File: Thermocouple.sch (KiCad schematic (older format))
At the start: 0 parts

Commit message: Blocked out the thermocouple worksheet
Added the instrumentation amplifier, ADC placeholder and general
temperature sensor placeholder.
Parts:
- added C?: C, ~, symbol C
- added D?: ZENER, ~, symbol ZENER
- added R? (x7): R, ~, symbol R
- added U? (x4): LM324, symbol LM324
- added U? (x2): MCP3550-60-E/SN, SO8, symbol MCP3550-60-E/SN
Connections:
- net labels added: +12V, -12V, AGND
- wire segments 0 -> 42
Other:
- note added: "16-24bit ADC\n\nIdeally, a two channel ADC, rather than\ntwo separate, discreet components: this \nand the device above."
- note added: "Acting as an instrumentation opamp"
- note added: "Input from physical \nthermocouple connector\n"
- note added: "Input from physical\nthermocouple connector\n"
- note added: "Zener placeholder for \ngeneral temperature sensor\n"

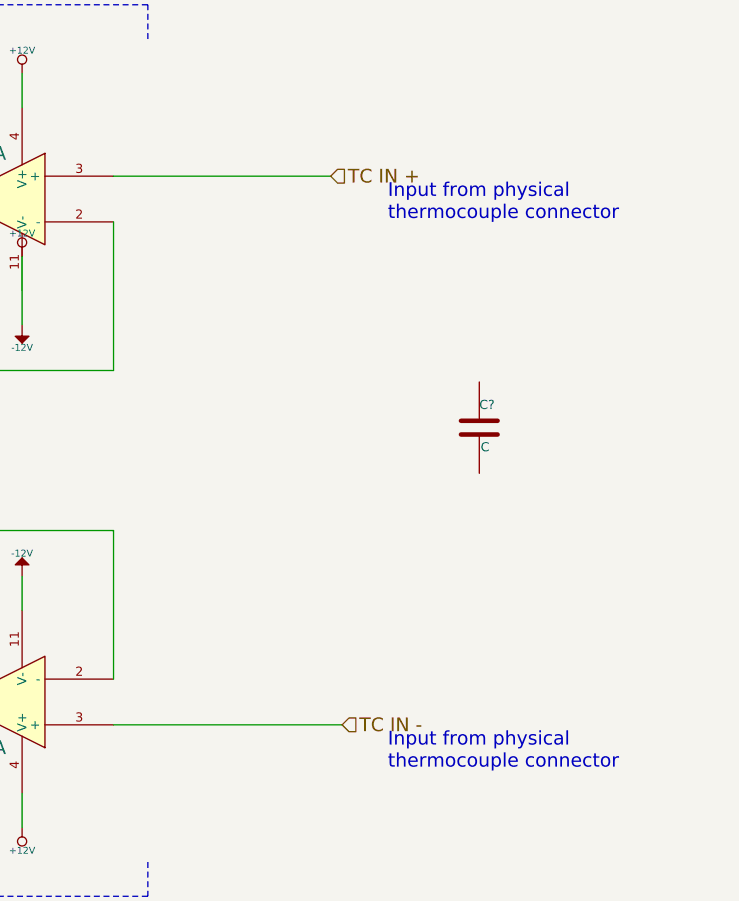
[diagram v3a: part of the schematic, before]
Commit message: Completed Arduino Block Diagram and Fan Redesign
The commits as of this are now up to date with the videos released for
Contextual Electronics, Week 3.
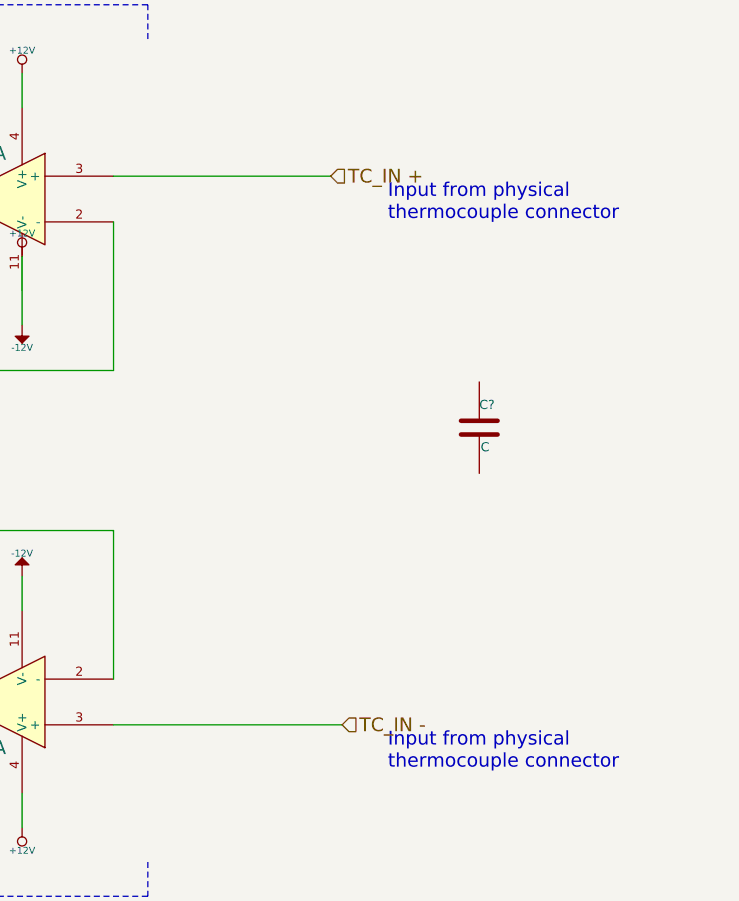
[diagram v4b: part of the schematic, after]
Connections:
- net labels added: TC_IN +, TC_IN -
- net labels removed: TC IN +, TC IN -
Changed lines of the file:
@@
 $Descr A4 11693 8268
 encoding utf-8
-Sheet 3 9
+Sheet 2 9
 Title ""
 Date "6 feb 2014"
@@
 $EndDescr
 Text HLabel 9100 2100 2    60   Input ~ 0
-TC IN +
+TC_IN +
 Text HLabel 9150 4500 2    60   Input ~ 0
-TC IN -
+TC_IN -
 Text HLabel 2050 3050 0    60   Input ~ 0
 MOSI

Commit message: Initial layout of relay and thermocouple
All block diagrams completed through Week 3.  Component selection
spreadsheets created: Bench Buddy Session 1CE.xlsx = official part
selection and bom.xlsx is the version I came up with.

Part association and initial layout of the Relay and Thermocouple
sections completed.
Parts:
- removed D?: ZENER, ~, symbol ZENER
- removed U?: LM324, symbol LM324
- removed U? (x2): MCP3550-60-E/SN, SO8, symbol MCP3550-60-E/SN
- added C1, C2, C4, C5, C6: C, ~, symbol C
- added P1: CONN_2, symbol CONN_2
- added P2: CONN_3X2, symbol CONN_3X2
- added R7, R9: R, ~, symbol R
- added U1: MCP3901, ~, symbol MCP3901
- added U3: LMT84, symbol LMT84
- U2: renamed from U?; value LM324 -> OPA4170; Distrib Part Num 1 (none) -> 296-29664-1; Distrib Part Num 1 Link (none) -> http://www.digikey.com/product-detail/en/OPA4170AIDR/296-29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; MFG Name (none) -> Texas Instruments; MFG Part Num (none) -> OPA4170AIDR
- gave numbers to parts that had none: 8
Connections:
- net labels added: +5V, REF+, REF-, ~CS, ~DR, ~RESET
- net labels removed: CS_N
- wire segments 42 -> 88
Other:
- note added: "Analog Front End\n\nActing as a 16-bit ADC"
- note added: "LMT84 Temperature Sensor\nas Cold Junction Reference"
- note added: "OPA4170 acting as an instrumentation opamp"
- note removed: "16-24bit ADC\n\nIdeally, a two channel ADC, rather than\ntwo separate, discreet components: this \nand the device above."
- note removed: "Acting as an instrumentation opamp"
- note removed: "Zener placeholder for \ngeneral temperature sensor\n"
- moved on the sheet: C3, R1, R2, R8

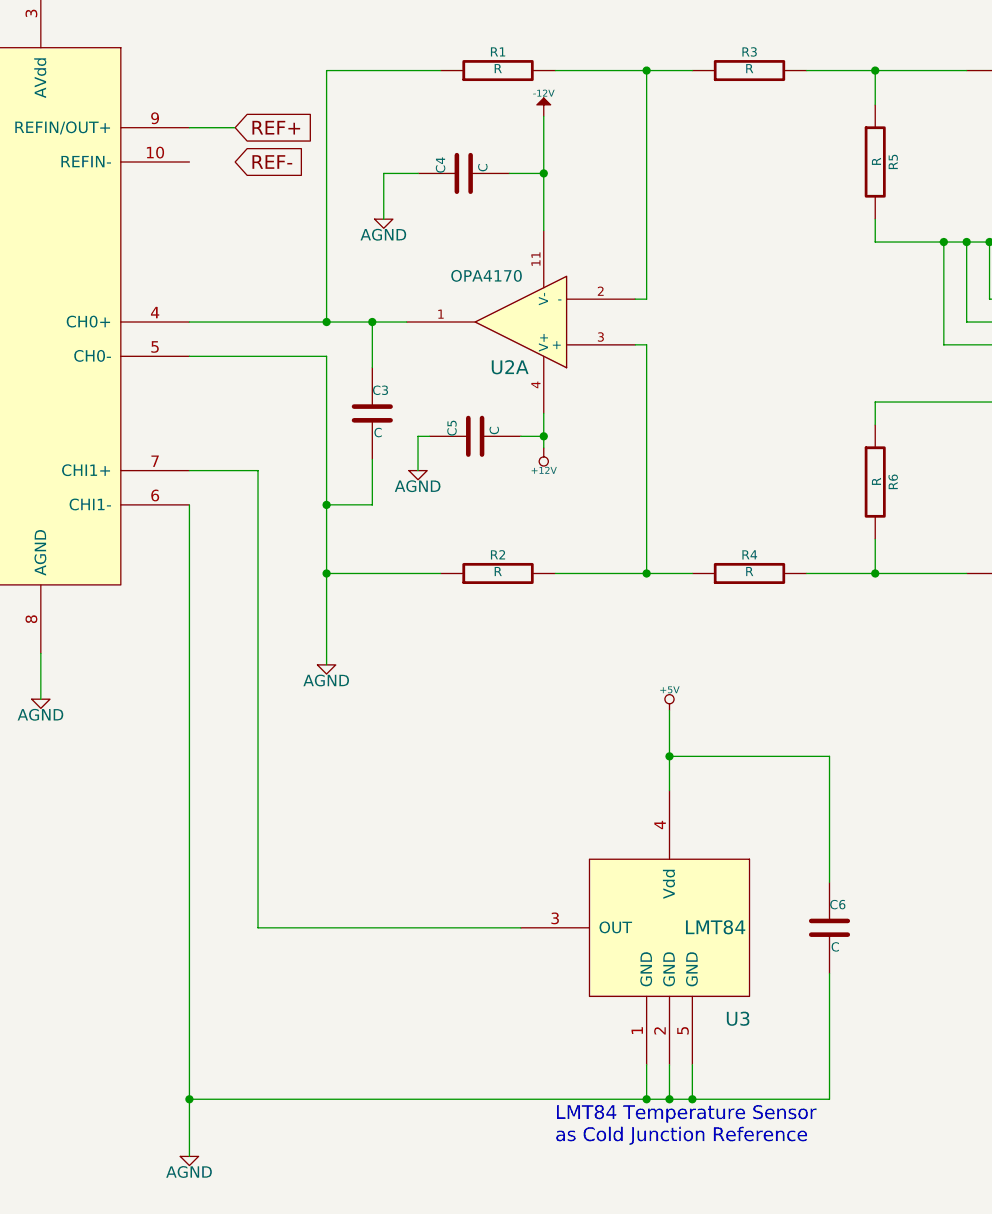
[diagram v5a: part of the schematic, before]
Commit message: Initial layout of Arduino and Fan-Current
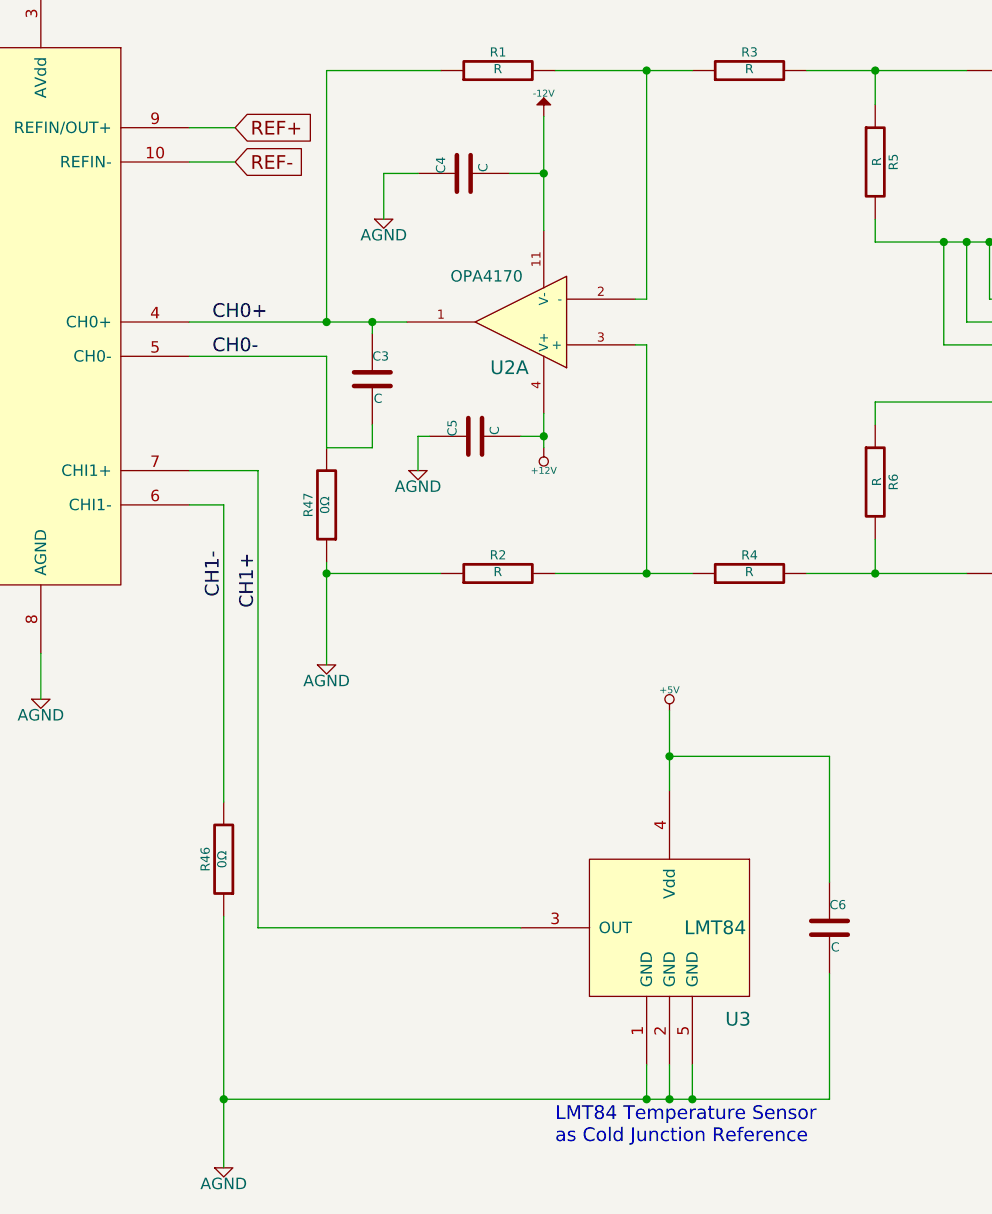
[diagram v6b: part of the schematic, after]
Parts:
- added R46, R47: 0Ω, ~, symbol R
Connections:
- net AGND: now also R46.1, R47.1; no longer C3.2, U1.5 (CH0-), U1.6 (CHI1-)
- net REF-: now also U1.10 (REFIN-)
- net CH0+: now reaches C3.1, R1.1, U1.4 (CH0+), U2.1
- net CH1+: now reaches U1.7 (CHI1+), U3.3 (OUT)
- new net CH0-: C3.2, R47.2, U1.5 (CH0-)
- new net CH1-: R46.2, U1.6 (CHI1-)
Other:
- moved on the sheet: C3
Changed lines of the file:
@@
 Sheet 2 9
 Title ""
-Date "21 feb 2014"
+Date "22 feb 2014"
 Rev ""
 Comp ""
@@
 L C C3
 U 1 1 52F12CBA
-P 4550 3700
-F 0 "C3" H 4550 3800 40  0000 L CNN
-F 1 "C" H 4556 3615 40  0000 L CNN
-F 2 "~" H 4588 3550 30  0000 C CNN
-F 3 "~" H 4550 3700 60  0000 C CNN
-	1    4550 3700
+P 4550 3550
+F 0 "C3" H 4550 3650 40  0000 L CNN
+F 1 "C" H 4556 3465 40  0000 L CNN
+F 2 "~" H 4588 3400 30  0000 C CNN
+F 3 "~" H 4550 3550 60  0000 C CNN
+	1    4550 3550
 	1    0    0    -1
 $EndComp
@@
 L AGND #PWR08
 U 1 1 5306EB85
-P 3750 6950
-F 0 "#PWR08" H 3750 6950 40  0001 C CNN
-F 1 "AGND" H 3750 6880 50  0000 C CNN
-F 2 "" H 3750 6950 60  0000 C CNN
-F 3 "" H 3750 6950 60  0000 C CNN
-	1    3750 6950
+P 3900 7000
+F 0 "#PWR08" H 3900 7000 40  0001 C CNN
+F 1 "AGND" H 3900 6930 50  0000 C CNN
+F 2 "" H 3900 7000 60  0000 C CNN
+F 3 "" H 3900 7000 60  0000 C CNN
+	1    3900 7000
 	1    0    0    -1
 $EndComp
@@
 	4350 4400 4850 4400
 Wire Wire Line
-	4350 3450 4350 4800
-Wire Wire Line
 	4350 2200 4850 2200
 Wire Wire Line
@@
 Wire Wire Line
 	7750 2750 7750 2600
-Connection ~ 4350 4100
-Wire Wire Line
-	4550 3300 4550 3500
+Wire Wire Line
+	4550 3300 4550 3350
 Connection ~ 4550 3300
 Wire Wire Line
-	4350 4100 4550 4100
-Wire Wire Line
-	4550 4100 4550 3900
+	4550 3850 4550 3750
 Wire Wire Line
 	5200 5950 4050 5950
@@
 Wire Wire Line
 	4050 3950 3750 3950
-Wire Wire Line
-	3750 4100 3750 6950
-Wire Wire Line
-	3750 6700 6550 6700
 Wire Wire Line
 	5750 6700 5750 6550
@@
 	5950 6700 5950 6550
 Connection ~ 5850 6700
-Connection ~ 3750 6700
 Wire Wire Line
 	5850 5000 5850 5350
@@
 	-1   0    0    -1
 $EndComp
+Wire Wire Line
+	3950 2600 3750 2600
+Text Label 3850 3300 0    60   ~ 0
+CH0+
+Text Label 3850 3450 0    60   ~ 0
+CH0-
+Wire Wire Line
+	3750 4100 3900 4100
+Wire Wire Line
+	3900 6700 6550 6700
+Connection ~ 3900 6700
+Text Label 3900 4300 3    60   ~ 0
+CH1-
+Text Label 4050 4550 1    60   ~ 0
+CH1+
+$Comp
+L R R47
+U 1 1 53078EA2
+P 4350 4100
+F 0 "R47" V 4430 4100 40  0000 C CNN
+F 1 "0Ω" V 4357 4101 40  0000 C CNN
+F 2 "~" V 4280 4100 30  0000 C CNN
+F 3 "~" H 4350 4100 30  0000 C CNN
+	1    4350 4100
+	-1   0    0    1
+$EndComp
+Wire Wire Line
+	4550 3850 4350 3850
+Wire Wire Line
+	4350 3850 4350 3450
+Wire Wire Line
+	4350 4350 4350 4800
+$Comp
+L R R46
+U 1 1 5307912D
+P 3900 5650
+F 0 "R46" V 3980 5650 40  0000 C CNN
+F 1 "0Ω" V 3907 5651 40  0000 C CNN
+F 2 "~" V 3830 5650 30  0000 C CNN
+F 3 "~" H 3900 5650 30  0000 C CNN
+	1    3900 5650
+	-1   0    0    1
+$EndComp
+Wire Wire Line
+	3900 4100 3900 5400
+Wire Wire Line
+	3900 5900 3900 7000
 $EndSCHEMATC

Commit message: Reorganization of power conditioning module
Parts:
- U1: Distrib Part Num 1 (none) -> MCP3901A0-I/SS; Distrib Part Num 1 Link (none) -> http://www.microchip.com/mymicrochip/filehandler.aspx?ddocn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; MFG Name (none) -> Microchip Tech; MFG Part Num (none) -> MCP3901A0-I/SS
- U3: Distrib Part Num 1 (none) -> 296-35727-2; Distrib Part Num 1 Link (none) -> http://www.ti.com/lit/ds/symlink/lmt84.pdf; MFG Name (none) -> Texas Instruments; MFG Part Num (none) -> LMT84DCKT
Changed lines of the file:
@@
 F 2 "" H 5850 5950 60  0000 C CNN
 F 3 "" H 5850 5950 60  0000 C CNN
+F 4 "Texas Instruments" H 5850 5950 60  0001 C CNN "MFG Name"
+F 5 "LMT84DCKT" H 5850 5950 60  0001 C CNN "MFG Part Num"
+F 6 "296-35727-2" H 5850 5950 60  0001 C CNN "Distrib Part Num 1"
+F 7 "http://www.ti.com/lit/ds/symlink/lmt84.pdf" H 5850 5950 60  0001 C CNN "Distrib Part Num 1 Link"
 	1    5850 5950
 	1    0    0    -1
@@
 F 2 "~" H 2900 3750 60  0000 C CNN
 F 3 "~" H 2900 3750 60  0000 C CNN
+F 4 "Microchip Tech" H 2800 3300 60  0001 C CNN "MFG Name"
+F 5 "MCP3901A0-I/SS" H 2800 3300 60  0001 C CNN "MFG Part Num"
+F 6 "MCP3901A0-I/SS" H 2800 3300 60  0001 C CNN "Distrib Part Num 1"
+F 7 "http://www.microchip.com/mymicrochip/filehandler.aspx?ddocname=en545016" H 2800 3300 60  0001 C CNN "Distrib Part Num 1 Link"
 	1    2800 3300
 	-1   0    0    -1
